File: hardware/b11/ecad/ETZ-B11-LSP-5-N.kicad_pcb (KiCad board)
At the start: 2 copper layers, 144.7 x 90.2 mm, 0 parts

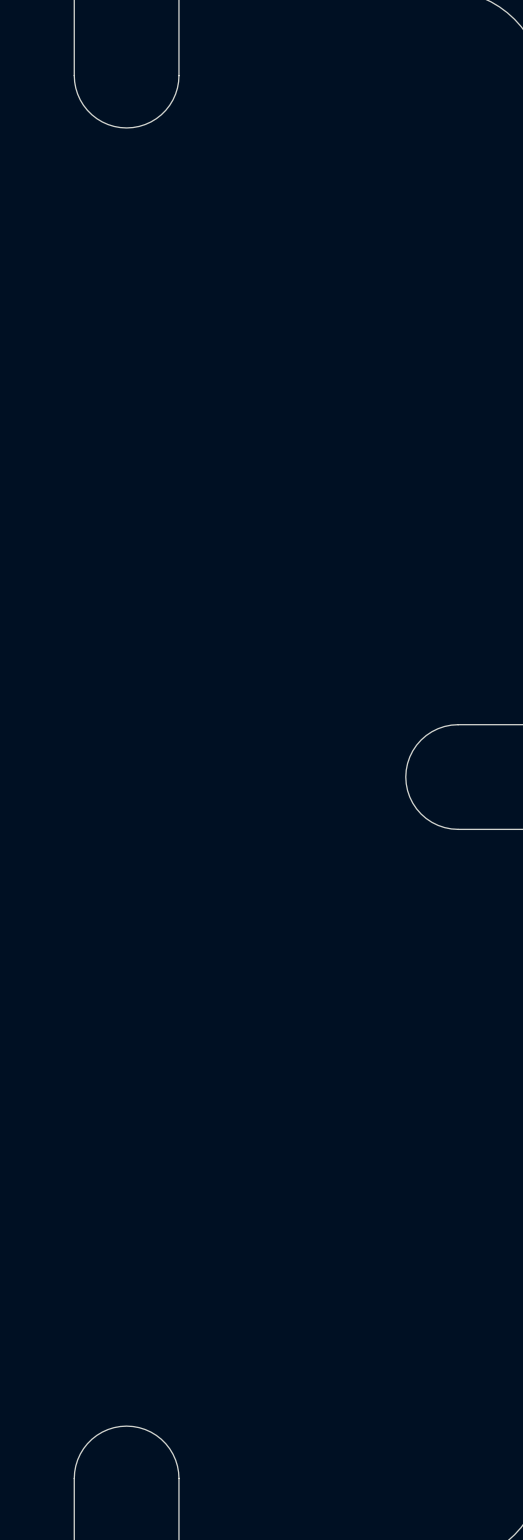
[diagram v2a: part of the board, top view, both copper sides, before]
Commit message: feat(hardware/b11): populate component placements across all carrier PCBs
KiCad serialized full footprint and component placement data for all
four carrier board variants after interactive editing session.

Co-Authored-By: Claude Sonnet 4.6 <noreply@anthropic.com>
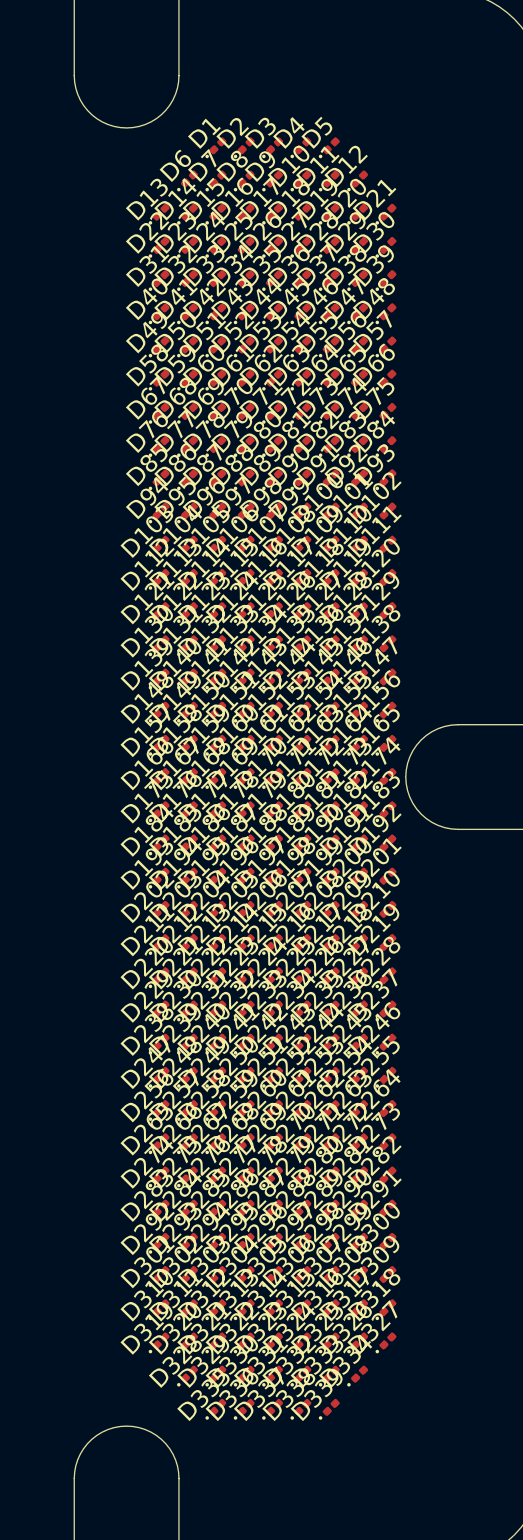
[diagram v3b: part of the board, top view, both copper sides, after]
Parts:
- added D1: LED_0201_0603Metric, LED_0201_0603Metric, F.Cu at (202.2, 68.1)
- added D10: LED_0201_0603Metric, LED_0201_0603Metric, F.Cu at (207.1, 70.0)
- added D100: LED_0201_0603Metric, LED_0201_0603Metric, F.Cu at (208.7, 89.1)
- added D101: LED_0201_0603Metric, LED_0201_0603Metric, F.Cu at (210.3, 89.1)
- added D102: LED_0201_0603Metric, LED_0201_0603Metric, F.Cu at (211.9, 89.1)
- added D103: LED_0201_0603Metric, LED_0201_0603Metric, F.Cu at (198.9, 91.0)
- added D104: LED_0201_0603Metric, LED_0201_0603Metric, F.Cu at (200.6, 91.0)
- added D105: LED_0201_0603Metric, LED_0201_0603Metric, F.Cu at (202.2, 91.0)
- added D106: LED_0201_0603Metric, LED_0201_0603Metric, F.Cu at (203.8, 91.0)
- added D107: LED_0201_0603Metric, LED_0201_0603Metric, F.Cu at (205.4, 91.0)
- added D108: LED_0201_0603Metric, LED_0201_0603Metric, F.Cu at (207.1, 91.0)
- added D109: LED_0201_0603Metric, LED_0201_0603Metric, F.Cu at (208.7, 91.0)
- added D11: LED_0201_0603Metric, LED_0201_0603Metric, F.Cu at (208.7, 70.0)
- added D110: LED_0201_0603Metric, LED_0201_0603Metric, F.Cu at (210.3, 91.0)
- added D111: LED_0201_0603Metric, LED_0201_0603Metric, F.Cu at (211.9, 91.0)
- added D112: LED_0201_0603Metric, LED_0201_0603Metric, F.Cu at (198.9, 92.9)
- added D113: LED_0201_0603Metric, LED_0201_0603Metric, F.Cu at (200.6, 92.9)
- added D114: LED_0201_0603Metric, LED_0201_0603Metric, F.Cu at (202.2, 92.9)
- added D115: LED_0201_0603Metric, LED_0201_0603Metric, F.Cu at (203.8, 92.9)
- added D116: LED_0201_0603Metric, LED_0201_0603Metric, F.Cu at (205.4, 92.9)
- added D117: LED_0201_0603Metric, LED_0201_0603Metric, F.Cu at (207.1, 92.9)
- added D118: LED_0201_0603Metric, LED_0201_0603Metric, F.Cu at (208.7, 92.9)
- added D119: LED_0201_0603Metric, LED_0201_0603Metric, F.Cu at (210.3, 92.9)
- added D12: LED_0201_0603Metric, LED_0201_0603Metric, F.Cu at (210.3, 70.0)
- added D120: LED_0201_0603Metric, LED_0201_0603Metric, F.Cu at (211.9, 92.9)
- added D121: LED_0201_0603Metric, LED_0201_0603Metric, F.Cu at (198.9, 94.8)
- added D122: LED_0201_0603Metric, LED_0201_0603Metric, F.Cu at (200.6, 94.8)
- added D123: LED_0201_0603Metric, LED_0201_0603Metric, F.Cu at (202.2, 94.8)
- added D124: LED_0201_0603Metric, LED_0201_0603Metric, F.Cu at (203.8, 94.8)
- added D125: LED_0201_0603Metric, LED_0201_0603Metric, F.Cu at (205.4, 94.8)
- added D126: LED_0201_0603Metric, LED_0201_0603Metric, F.Cu at (207.1, 94.8)
- added D127: LED_0201_0603Metric, LED_0201_0603Metric, F.Cu at (208.7, 94.8)
- added D128: LED_0201_0603Metric, LED_0201_0603Metric, F.Cu at (210.3, 94.8)
- added D129: LED_0201_0603Metric, LED_0201_0603Metric, F.Cu at (211.9, 94.8)
- added D13: LED_0201_0603Metric, LED_0201_0603Metric, F.Cu at (198.9, 71.9)
- added D130: LED_0201_0603Metric, LED_0201_0603Metric, F.Cu at (198.9, 96.7)
- added D131: LED_0201_0603Metric, LED_0201_0603Metric, F.Cu at (200.6, 96.7)
- added D132: LED_0201_0603Metric, LED_0201_0603Metric, F.Cu at (202.2, 96.7)
- added D133: LED_0201_0603Metric, LED_0201_0603Metric, F.Cu at (203.8, 96.7)
- added D134: LED_0201_0603Metric, LED_0201_0603Metric, F.Cu at (205.4, 96.7)
- added D135: LED_0201_0603Metric, LED_0201_0603Metric, F.Cu at (207.1, 96.7)
- added D136: LED_0201_0603Metric, LED_0201_0603Metric, F.Cu at (208.7, 96.7)
- added D137: LED_0201_0603Metric, LED_0201_0603Metric, F.Cu at (210.3, 96.7)
- added D138: LED_0201_0603Metric, LED_0201_0603Metric, F.Cu at (211.9, 96.7)
- added D139: LED_0201_0603Metric, LED_0201_0603Metric, F.Cu at (198.9, 98.6)
- added D14: LED_0201_0603Metric, LED_0201_0603Metric, F.Cu at (200.6, 71.9)
- added D140: LED_0201_0603Metric, LED_0201_0603Metric, F.Cu at (200.6, 98.6)
- added D141: LED_0201_0603Metric, LED_0201_0603Metric, F.Cu at (202.2, 98.6)
- added D142: LED_0201_0603Metric, LED_0201_0603Metric, F.Cu at (203.8, 98.6)
- added D143: LED_0201_0603Metric, LED_0201_0603Metric, F.Cu at (205.4, 98.6)
- added D144: LED_0201_0603Metric, LED_0201_0603Metric, F.Cu at (207.1, 98.6)
- added D145: LED_0201_0603Metric, LED_0201_0603Metric, F.Cu at (208.7, 98.6)
- added D146: LED_0201_0603Metric, LED_0201_0603Metric, F.Cu at (210.3, 98.6)
- added D147: LED_0201_0603Metric, LED_0201_0603Metric, F.Cu at (211.9, 98.6)
- added D148: LED_0201_0603Metric, LED_0201_0603Metric, F.Cu at (198.9, 100.5)
- added D149: LED_0201_0603Metric, LED_0201_0603Metric, F.Cu at (200.6, 100.5)
- added D15: LED_0201_0603Metric, LED_0201_0603Metric, F.Cu at (202.2, 71.9)
- added D150: LED_0201_0603Metric, LED_0201_0603Metric, F.Cu at (202.2, 100.5)
- added D151: LED_0201_0603Metric, LED_0201_0603Metric, F.Cu at (203.8, 100.5)
- added D152: LED_0201_0603Metric, LED_0201_0603Metric, F.Cu at (205.4, 100.5)
- added D153: LED_0201_0603Metric, LED_0201_0603Metric, F.Cu at (207.1, 100.5)
- added D154: LED_0201_0603Metric, LED_0201_0603Metric, F.Cu at (208.7, 100.5)
- added D155: LED_0201_0603Metric, LED_0201_0603Metric, F.Cu at (210.3, 100.5)
- added D156: LED_0201_0603Metric, LED_0201_0603Metric, F.Cu at (211.9, 100.5)
- added D157: LED_0201_0603Metric, LED_0201_0603Metric, F.Cu at (198.9, 102.4)
- added D158: LED_0201_0603Metric, LED_0201_0603Metric, F.Cu at (200.6, 102.4)
- added D159: LED_0201_0603Metric, LED_0201_0603Metric, F.Cu at (202.2, 102.4)
- added D16: LED_0201_0603Metric, LED_0201_0603Metric, F.Cu at (203.8, 71.9)
- added D160: LED_0201_0603Metric, LED_0201_0603Metric, F.Cu at (203.8, 102.4)
- added D161: LED_0201_0603Metric, LED_0201_0603Metric, F.Cu at (205.4, 102.4)
- added D162: LED_0201_0603Metric, LED_0201_0603Metric, F.Cu at (207.1, 102.4)
- added D163: LED_0201_0603Metric, LED_0201_0603Metric, F.Cu at (208.7, 102.4)
- added D164: LED_0201_0603Metric, LED_0201_0603Metric, F.Cu at (210.3, 102.4)
- added D165: LED_0201_0603Metric, LED_0201_0603Metric, F.Cu at (211.9, 102.4)
- added D166: LED_0201_0603Metric, LED_0201_0603Metric, F.Cu at (198.9, 104.3)
- added D167: LED_0201_0603Metric, LED_0201_0603Metric, F.Cu at (200.6, 104.3)
- added D168: LED_0201_0603Metric, LED_0201_0603Metric, F.Cu at (202.2, 104.3)
- added D169: LED_0201_0603Metric, LED_0201_0603Metric, F.Cu at (203.8, 104.3)
- added D17: LED_0201_0603Metric, LED_0201_0603Metric, F.Cu at (205.4, 71.9)
- added D170: LED_0201_0603Metric, LED_0201_0603Metric, F.Cu at (205.4, 104.3)
- added D171: LED_0201_0603Metric, LED_0201_0603Metric, F.Cu at (207.1, 104.3)
- added D172: LED_0201_0603Metric, LED_0201_0603Metric, F.Cu at (208.7, 104.3)
- added D173: LED_0201_0603Metric, LED_0201_0603Metric, F.Cu at (210.3, 104.3)
- added D174: LED_0201_0603Metric, LED_0201_0603Metric, F.Cu at (211.9, 104.3)
- added D175: LED_0201_0603Metric, LED_0201_0603Metric, F.Cu at (198.9, 106.2)
- added D176: LED_0201_0603Metric, LED_0201_0603Metric, F.Cu at (200.6, 106.2)
- added D177: LED_0201_0603Metric, LED_0201_0603Metric, F.Cu at (202.2, 106.2)
- added D178: LED_0201_0603Metric, LED_0201_0603Metric, F.Cu at (203.8, 106.2)
- added D179: LED_0201_0603Metric, LED_0201_0603Metric, F.Cu at (205.4, 106.2)
- added D18: LED_0201_0603Metric, LED_0201_0603Metric, F.Cu at (207.1, 71.9)
- added D180: LED_0201_0603Metric, LED_0201_0603Metric, F.Cu at (207.1, 106.2)
- added D181: LED_0201_0603Metric, LED_0201_0603Metric, F.Cu at (208.7, 106.2)
- added D182: LED_0201_0603Metric, LED_0201_0603Metric, F.Cu at (210.3, 106.2)
- added D183: LED_0201_0603Metric, LED_0201_0603Metric, F.Cu at (211.9, 106.2)
- added D184: LED_0201_0603Metric, LED_0201_0603Metric, F.Cu at (198.9, 108.1)
- added D185: LED_0201_0603Metric, LED_0201_0603Metric, F.Cu at (200.6, 108.1)
- added D186: LED_0201_0603Metric, LED_0201_0603Metric, F.Cu at (202.2, 108.1)
- added D187: LED_0201_0603Metric, LED_0201_0603Metric, F.Cu at (203.8, 108.1)
- added D188: LED_0201_0603Metric, LED_0201_0603Metric, F.Cu at (205.4, 108.1)
- added D189: LED_0201_0603Metric, LED_0201_0603Metric, F.Cu at (207.1, 108.1)
- added D19: LED_0201_0603Metric, LED_0201_0603Metric, F.Cu at (208.7, 71.9)
- added D190: LED_0201_0603Metric, LED_0201_0603Metric, F.Cu at (208.7, 108.1)
- added D191: LED_0201_0603Metric, LED_0201_0603Metric, F.Cu at (210.3, 108.1)
- added D192: LED_0201_0603Metric, LED_0201_0603Metric, F.Cu at (211.9, 108.1)
- added D193: LED_0201_0603Metric, LED_0201_0603Metric, F.Cu at (198.9, 110.0)
- added D194: LED_0201_0603Metric, LED_0201_0603Metric, F.Cu at (200.6, 110.0)
- added D195: LED_0201_0603Metric, LED_0201_0603Metric, F.Cu at (202.2, 110.0)
- added D196: LED_0201_0603Metric, LED_0201_0603Metric, F.Cu at (203.8, 110.0)
- added D197: LED_0201_0603Metric, LED_0201_0603Metric, F.Cu at (205.4, 110.0)
- added D198: LED_0201_0603Metric, LED_0201_0603Metric, F.Cu at (207.1, 110.0)
- added D199: LED_0201_0603Metric, LED_0201_0603Metric, F.Cu at (208.7, 110.0)
- added D2: LED_0201_0603Metric, LED_0201_0603Metric, F.Cu at (203.8, 68.1)
- added D20: LED_0201_0603Metric, LED_0201_0603Metric, F.Cu at (210.3, 71.9)
- added D200: LED_0201_0603Metric, LED_0201_0603Metric, F.Cu at (210.3, 110.0)
- added D201: LED_0201_0603Metric, LED_0201_0603Metric, F.Cu at (211.9, 110.0)
- added D202: LED_0201_0603Metric, LED_0201_0603Metric, F.Cu at (198.9, 111.9)
- added D203: LED_0201_0603Metric, LED_0201_0603Metric, F.Cu at (200.6, 111.9)
- added D204: LED_0201_0603Metric, LED_0201_0603Metric, F.Cu at (202.2, 111.9)
- added D205: LED_0201_0603Metric, LED_0201_0603Metric, F.Cu at (203.8, 111.9)
- added D206: LED_0201_0603Metric, LED_0201_0603Metric, F.Cu at (205.4, 111.9)
- added D207: LED_0201_0603Metric, LED_0201_0603Metric, F.Cu at (207.1, 111.9)
- added D208: LED_0201_0603Metric, LED_0201_0603Metric, F.Cu at (208.7, 111.9)
- added D209: LED_0201_0603Metric, LED_0201_0603Metric, F.Cu at (210.3, 111.9)
- added D21: LED_0201_0603Metric, LED_0201_0603Metric, F.Cu at (211.9, 71.9)
- added D210: LED_0201_0603Metric, LED_0201_0603Metric, F.Cu at (211.9, 111.9)
- added D211: LED_0201_0603Metric, LED_0201_0603Metric, F.Cu at (198.9, 113.8)
- added D212: LED_0201_0603Metric, LED_0201_0603Metric, F.Cu at (200.6, 113.8)
- added D213: LED_0201_0603Metric, LED_0201_0603Metric, F.Cu at (202.2, 113.8)
- added D214: LED_0201_0603Metric, LED_0201_0603Metric, F.Cu at (203.8, 113.8)
- added D215: LED_0201_0603Metric, LED_0201_0603Metric, F.Cu at (205.4, 113.8)
- added D216: LED_0201_0603Metric, LED_0201_0603Metric, F.Cu at (207.1, 113.8)
- added D217: LED_0201_0603Metric, LED_0201_0603Metric, F.Cu at (208.7, 113.8)
- added D218: LED_0201_0603Metric, LED_0201_0603Metric, F.Cu at (210.3, 113.8)
- added D219: LED_0201_0603Metric, LED_0201_0603Metric, F.Cu at (211.9, 113.8)
- added D22: LED_0201_0603Metric, LED_0201_0603Metric, F.Cu at (198.9, 73.8)
- added D220: LED_0201_0603Metric, LED_0201_0603Metric, F.Cu at (198.9, 115.7)
- added D221: LED_0201_0603Metric, LED_0201_0603Metric, F.Cu at (200.6, 115.7)
- added D222: LED_0201_0603Metric, LED_0201_0603Metric, F.Cu at (202.2, 115.7)
- added D223: LED_0201_0603Metric, LED_0201_0603Metric, F.Cu at (203.8, 115.7)
- added D224: LED_0201_0603Metric, LED_0201_0603Metric, F.Cu at (205.4, 115.7)
- added D225: LED_0201_0603Metric, LED_0201_0603Metric, F.Cu at (207.1, 115.7)
- added D226: LED_0201_0603Metric, LED_0201_0603Metric, F.Cu at (208.7, 115.7)
- added D227: LED_0201_0603Metric, LED_0201_0603Metric, F.Cu at (210.3, 115.7)
- added D228: LED_0201_0603Metric, LED_0201_0603Metric, F.Cu at (211.9, 115.7)
- added D229: LED_0201_0603Metric, LED_0201_0603Metric, F.Cu at (198.9, 117.6)
- added D23: LED_0201_0603Metric, LED_0201_0603Metric, F.Cu at (200.6, 73.8)
- added D230: LED_0201_0603Metric, LED_0201_0603Metric, F.Cu at (200.6, 117.6)
- added D231: LED_0201_0603Metric, LED_0201_0603Metric, F.Cu at (202.2, 117.6)
- added D232: LED_0201_0603Metric, LED_0201_0603Metric, F.Cu at (203.8, 117.6)
- added D233: LED_0201_0603Metric, LED_0201_0603Metric, F.Cu at (205.4, 117.6)
- added D234: LED_0201_0603Metric, LED_0201_0603Metric, F.Cu at (207.1, 117.6)
- added D235: LED_0201_0603Metric, LED_0201_0603Metric, F.Cu at (208.7, 117.6)
- added D236: LED_0201_0603Metric, LED_0201_0603Metric, F.Cu at (210.3, 117.6)
- added D237: LED_0201_0603Metric, LED_0201_0603Metric, F.Cu at (211.9, 117.6)
- added D238: LED_0201_0603Metric, LED_0201_0603Metric, F.Cu at (198.9, 119.5)
- added D239: LED_0201_0603Metric, LED_0201_0603Metric, F.Cu at (200.6, 119.5)
- added D24: LED_0201_0603Metric, LED_0201_0603Metric, F.Cu at (202.2, 73.8)
- added D240: LED_0201_0603Metric, LED_0201_0603Metric, F.Cu at (202.2, 119.5)
- added D241: LED_0201_0603Metric, LED_0201_0603Metric, F.Cu at (203.8, 119.5)
- added D242: LED_0201_0603Metric, LED_0201_0603Metric, F.Cu at (205.4, 119.5)
- added D243: LED_0201_0603Metric, LED_0201_0603Metric, F.Cu at (207.1, 119.5)
- added D244: LED_0201_0603Metric, LED_0201_0603Metric, F.Cu at (208.7, 119.5)
- added D245: LED_0201_0603Metric, LED_0201_0603Metric, F.Cu at (210.3, 119.5)
- added D246: LED_0201_0603Metric, LED_0201_0603Metric, F.Cu at (211.9, 119.5)
- added D247: LED_0201_0603Metric, LED_0201_0603Metric, F.Cu at (198.9, 121.4)
- added D248: LED_0201_0603Metric, LED_0201_0603Metric, F.Cu at (200.6, 121.4)
- added D249: LED_0201_0603Metric, LED_0201_0603Metric, F.Cu at (202.2, 121.4)
- added D25: LED_0201_0603Metric, LED_0201_0603Metric, F.Cu at (203.8, 73.8)
- added D250: LED_0201_0603Metric, LED_0201_0603Metric, F.Cu at (203.8, 121.4)
- added D251: LED_0201_0603Metric, LED_0201_0603Metric, F.Cu at (205.4, 121.4)
- added D252: LED_0201_0603Metric, LED_0201_0603Metric, F.Cu at (207.1, 121.4)
- added D253: LED_0201_0603Metric, LED_0201_0603Metric, F.Cu at (208.7, 121.4)
- added D254: LED_0201_0603Metric, LED_0201_0603Metric, F.Cu at (210.3, 121.4)
- added D255: LED_0201_0603Metric, LED_0201_0603Metric, F.Cu at (211.9, 121.4)
- added D256: LED_0201_0603Metric, LED_0201_0603Metric, F.Cu at (198.9, 123.3)
- added D257: LED_0201_0603Metric, LED_0201_0603Metric, F.Cu at (200.6, 123.3)
- added D258: LED_0201_0603Metric, LED_0201_0603Metric, F.Cu at (202.2, 123.3)
- added D259: LED_0201_0603Metric, LED_0201_0603Metric, F.Cu at (203.8, 123.3)
- added D26: LED_0201_0603Metric, LED_0201_0603Metric, F.Cu at (205.4, 73.8)
- added D260: LED_0201_0603Metric, LED_0201_0603Metric, F.Cu at (205.4, 123.3)
- added D261: LED_0201_0603Metric, LED_0201_0603Metric, F.Cu at (207.1, 123.3)
- added D262: LED_0201_0603Metric, LED_0201_0603Metric, F.Cu at (208.7, 123.3)
- added D263: LED_0201_0603Metric, LED_0201_0603Metric, F.Cu at (210.3, 123.3)
- added D264: LED_0201_0603Metric, LED_0201_0603Metric, F.Cu at (211.9, 123.3)
- added D265: LED_0201_0603Metric, LED_0201_0603Metric, F.Cu at (198.9, 125.2)
- added D266: LED_0201_0603Metric, LED_0201_0603Metric, F.Cu at (200.6, 125.2)
- added D267: LED_0201_0603Metric, LED_0201_0603Metric, F.Cu at (202.2, 125.2)
- added D268: LED_0201_0603Metric, LED_0201_0603Metric, F.Cu at (203.8, 125.2)
- added D269: LED_0201_0603Metric, LED_0201_0603Metric, F.Cu at (205.4, 125.2)
- added D27: LED_0201_0603Metric, LED_0201_0603Metric, F.Cu at (207.1, 73.8)
- added D270: LED_0201_0603Metric, LED_0201_0603Metric, F.Cu at (207.1, 125.2)
- added D271: LED_0201_0603Metric, LED_0201_0603Metric, F.Cu at (208.7, 125.2)
- added D272: LED_0201_0603Metric, LED_0201_0603Metric, F.Cu at (210.3, 125.2)
- added D273: LED_0201_0603Metric, LED_0201_0603Metric, F.Cu at (211.9, 125.2)
- added D274: LED_0201_0603Metric, LED_0201_0603Metric, F.Cu at (198.9, 127.1)
- added D275: LED_0201_0603Metric, LED_0201_0603Metric, F.Cu at (200.6, 127.1)
- added D276: LED_0201_0603Metric, LED_0201_0603Metric, F.Cu at (202.2, 127.1)
- added D277: LED_0201_0603Metric, LED_0201_0603Metric, F.Cu at (203.8, 127.1)
- added D278: LED_0201_0603Metric, LED_0201_0603Metric, F.Cu at (205.4, 127.1)
- added D279: LED_0201_0603Metric, LED_0201_0603Metric, F.Cu at (207.1, 127.1)
- added D28: LED_0201_0603Metric, LED_0201_0603Metric, F.Cu at (208.7, 73.8)
- added D280: LED_0201_0603Metric, LED_0201_0603Metric, F.Cu at (208.7, 127.1)
- added D281: LED_0201_0603Metric, LED_0201_0603Metric, F.Cu at (210.3, 127.1)
- added D282: LED_0201_0603Metric, LED_0201_0603Metric, F.Cu at (211.9, 127.1)
- added D283: LED_0201_0603Metric, LED_0201_0603Metric, F.Cu at (198.9, 129.0)
- added D284: LED_0201_0603Metric, LED_0201_0603Metric, F.Cu at (200.6, 129.0)
- added D285: LED_0201_0603Metric, LED_0201_0603Metric, F.Cu at (202.2, 129.0)
- added D286: LED_0201_0603Metric, LED_0201_0603Metric, F.Cu at (203.8, 129.0)
- added D287: LED_0201_0603Metric, LED_0201_0603Metric, F.Cu at (205.4, 129.0)
- added D288: LED_0201_0603Metric, LED_0201_0603Metric, F.Cu at (207.1, 129.0)
- added D289: LED_0201_0603Metric, LED_0201_0603Metric, F.Cu at (208.7, 129.0)
- added D29: LED_0201_0603Metric, LED_0201_0603Metric, F.Cu at (210.3, 73.8)
- added D290: LED_0201_0603Metric, LED_0201_0603Metric, F.Cu at (210.3, 129.0)
- added D291: LED_0201_0603Metric, LED_0201_0603Metric, F.Cu at (211.9, 129.0)
- added D292: LED_0201_0603Metric, LED_0201_0603Metric, F.Cu at (198.9, 130.9)
- added D293: LED_0201_0603Metric, LED_0201_0603Metric, F.Cu at (200.6, 130.9)
- added D294: LED_0201_0603Metric, LED_0201_0603Metric, F.Cu at (202.2, 130.9)
- added D295: LED_0201_0603Metric, LED_0201_0603Metric, F.Cu at (203.8, 130.9)
- added D296: LED_0201_0603Metric, LED_0201_0603Metric, F.Cu at (205.4, 130.9)
- added D297: LED_0201_0603Metric, LED_0201_0603Metric, F.Cu at (207.1, 130.9)
- added D298: LED_0201_0603Metric, LED_0201_0603Metric, F.Cu at (208.7, 130.9)
- added D299: LED_0201_0603Metric, LED_0201_0603Metric, F.Cu at (210.3, 130.9)
- added D3: LED_0201_0603Metric, LED_0201_0603Metric, F.Cu at (205.4, 68.1)
- added D30: LED_0201_0603Metric, LED_0201_0603Metric, F.Cu at (211.9, 73.8)
- added D300: LED_0201_0603Metric, LED_0201_0603Metric, F.Cu at (211.9, 130.9)
- added D301: LED_0201_0603Metric, LED_0201_0603Metric, F.Cu at (198.9, 132.8)
- added D302: LED_0201_0603Metric, LED_0201_0603Metric, F.Cu at (200.6, 132.8)
- added D303: LED_0201_0603Metric, LED_0201_0603Metric, F.Cu at (202.2, 132.8)
- added D304: LED_0201_0603Metric, LED_0201_0603Metric, F.Cu at (203.8, 132.8)
- added D305: LED_0201_0603Metric, LED_0201_0603Metric, F.Cu at (205.4, 132.8)
- added D306: LED_0201_0603Metric, LED_0201_0603Metric, F.Cu at (207.1, 132.8)
- added D307: LED_0201_0603Metric, LED_0201_0603Metric, F.Cu at (208.7, 132.8)
- added D308: LED_0201_0603Metric, LED_0201_0603Metric, F.Cu at (210.3, 132.8)
- added D309: LED_0201_0603Metric, LED_0201_0603Metric, F.Cu at (211.9, 132.8)
- added D31: LED_0201_0603Metric, LED_0201_0603Metric, F.Cu at (198.9, 75.7)
- added D310: LED_0201_0603Metric, LED_0201_0603Metric, F.Cu at (198.9, 134.7)
- added D311: LED_0201_0603Metric, LED_0201_0603Metric, F.Cu at (200.6, 134.7)
- added D312: LED_0201_0603Metric, LED_0201_0603Metric, F.Cu at (202.2, 134.7)
- added D313: LED_0201_0603Metric, LED_0201_0603Metric, F.Cu at (203.8, 134.7)
- added D314: LED_0201_0603Metric, LED_0201_0603Metric, F.Cu at (205.4, 134.7)
- added D315: LED_0201_0603Metric, LED_0201_0603Metric, F.Cu at (207.1, 134.7)
- added D316: LED_0201_0603Metric, LED_0201_0603Metric, F.Cu at (208.7, 134.7)
- added D317: LED_0201_0603Metric, LED_0201_0603Metric, F.Cu at (210.3, 134.7)
- added D318: LED_0201_0603Metric, LED_0201_0603Metric, F.Cu at (211.9, 134.7)
- added D319: LED_0201_0603Metric, LED_0201_0603Metric, F.Cu at (198.9, 136.6)
- added D32: LED_0201_0603Metric, LED_0201_0603Metric, F.Cu at (200.6, 75.7)
- added D320: LED_0201_0603Metric, LED_0201_0603Metric, F.Cu at (200.6, 136.6)
- added D321: LED_0201_0603Metric, LED_0201_0603Metric, F.Cu at (202.2, 136.6)
- added D322: LED_0201_0603Metric, LED_0201_0603Metric, F.Cu at (203.8, 136.6)
- added D323: LED_0201_0603Metric, LED_0201_0603Metric, F.Cu at (205.4, 136.6)
- added D324: LED_0201_0603Metric, LED_0201_0603Metric, F.Cu at (207.1, 136.6)
- added D325: LED_0201_0603Metric, LED_0201_0603Metric, F.Cu at (208.7, 136.6)
- added D326: LED_0201_0603Metric, LED_0201_0603Metric, F.Cu at (210.3, 136.6)
- added D327: LED_0201_0603Metric, LED_0201_0603Metric, F.Cu at (211.9, 136.6)
- added D328: LED_0201_0603Metric, LED_0201_0603Metric, F.Cu at (200.6, 138.5)
- added D329: LED_0201_0603Metric, LED_0201_0603Metric, F.Cu at (202.2, 138.5)
- added D33: LED_0201_0603Metric, LED_0201_0603Metric, F.Cu at (202.2, 75.7)
- added D330: LED_0201_0603Metric, LED_0201_0603Metric, F.Cu at (203.8, 138.5)
- added D331: LED_0201_0603Metric, LED_0201_0603Metric, F.Cu at (205.4, 138.5)
- added D332: LED_0201_0603Metric, LED_0201_0603Metric, F.Cu at (207.1, 138.5)
- added D333: LED_0201_0603Metric, LED_0201_0603Metric, F.Cu at (208.7, 138.5)
- added D334: LED_0201_0603Metric, LED_0201_0603Metric, F.Cu at (210.3, 138.5)
- added D335: LED_0201_0603Metric, LED_0201_0603Metric, F.Cu at (202.2, 140.4)
- added D336: LED_0201_0603Metric, LED_0201_0603Metric, F.Cu at (203.8, 140.4)
- added D337: LED_0201_0603Metric, LED_0201_0603Metric, F.Cu at (205.4, 140.4)
- added D338: LED_0201_0603Metric, LED_0201_0603Metric, F.Cu at (207.1, 140.4)
- added D339: LED_0201_0603Metric, LED_0201_0603Metric, F.Cu at (208.7, 140.4)
- added D34: LED_0201_0603Metric, LED_0201_0603Metric, F.Cu at (203.8, 75.7)
- added D35: LED_0201_0603Metric, LED_0201_0603Metric, F.Cu at (205.4, 75.7)
- added D36: LED_0201_0603Metric, LED_0201_0603Metric, F.Cu at (207.1, 75.7)
- added D37: LED_0201_0603Metric, LED_0201_0603Metric, F.Cu at (208.7, 75.7)
- added D38: LED_0201_0603Metric, LED_0201_0603Metric, F.Cu at (210.3, 75.7)
- added D39: LED_0201_0603Metric, LED_0201_0603Metric, F.Cu at (211.9, 75.7)
- added D4: LED_0201_0603Metric, LED_0201_0603Metric, F.Cu at (207.1, 68.1)
- added D40: LED_0201_0603Metric, LED_0201_0603Metric, F.Cu at (198.9, 77.6)
- added D41: LED_0201_0603Metric, LED_0201_0603Metric, F.Cu at (200.6, 77.6)
- added D42: LED_0201_0603Metric, LED_0201_0603Metric, F.Cu at (202.2, 77.6)
- added D43: LED_0201_0603Metric, LED_0201_0603Metric, F.Cu at (203.8, 77.6)
- added D44: LED_0201_0603Metric, LED_0201_0603Metric, F.Cu at (205.4, 77.6)
- added D45: LED_0201_0603Metric, LED_0201_0603Metric, F.Cu at (207.1, 77.6)
- added D46: LED_0201_0603Metric, LED_0201_0603Metric, F.Cu at (208.7, 77.6)
- added D47: LED_0201_0603Metric, LED_0201_0603Metric, F.Cu at (210.3, 77.6)
- added D48: LED_0201_0603Metric, LED_0201_0603Metric, F.Cu at (211.9, 77.6)
- added D49: LED_0201_0603Metric, LED_0201_0603Metric, F.Cu at (198.9, 79.5)
- added D5: LED_0201_0603Metric, LED_0201_0603Metric, F.Cu at (208.7, 68.1)
- added D50: LED_0201_0603Metric, LED_0201_0603Metric, F.Cu at (200.6, 79.5)
- added D51: LED_0201_0603Metric, LED_0201_0603Metric, F.Cu at (202.2, 79.5)
- added D52: LED_0201_0603Metric, LED_0201_0603Metric, F.Cu at (203.8, 79.5)
- added D53: LED_0201_0603Metric, LED_0201_0603Metric, F.Cu at (205.4, 79.5)
- added D54: LED_0201_0603Metric, LED_0201_0603Metric, F.Cu at (207.1, 79.5)
- added D55: LED_0201_0603Metric, LED_0201_0603Metric, F.Cu at (208.7, 79.5)
- added D56: LED_0201_0603Metric, LED_0201_0603Metric, F.Cu at (210.3, 79.5)
- added D57: LED_0201_0603Metric, LED_0201_0603Metric, F.Cu at (211.9, 79.5)
- added D58: LED_0201_0603Metric, LED_0201_0603Metric, F.Cu at (198.9, 81.4)
- added D59: LED_0201_0603Metric, LED_0201_0603Metric, F.Cu at (200.6, 81.4)
- added D6: LED_0201_0603Metric, LED_0201_0603Metric, F.Cu at (200.6, 70.0)
- added D60: LED_0201_0603Metric, LED_0201_0603Metric, F.Cu at (202.2, 81.4)
- added D61: LED_0201_0603Metric, LED_0201_0603Metric, F.Cu at (203.8, 81.4)
- added D62: LED_0201_0603Metric, LED_0201_0603Metric, F.Cu at (205.4, 81.4)
- added D63: LED_0201_0603Metric, LED_0201_0603Metric, F.Cu at (207.1, 81.4)
- added D64: LED_0201_0603Metric, LED_0201_0603Metric, F.Cu at (208.7, 81.4)
- added D65: LED_0201_0603Metric, LED_0201_0603Metric, F.Cu at (210.3, 81.4)
- added D66: LED_0201_0603Metric, LED_0201_0603Metric, F.Cu at (211.9, 81.4)
- added D67: LED_0201_0603Metric, LED_0201_0603Metric, F.Cu at (198.9, 83.3)
- added D68: LED_0201_0603Metric, LED_0201_0603Metric, F.Cu at (200.6, 83.3)
- added D69: LED_0201_0603Metric, LED_0201_0603Metric, F.Cu at (202.2, 83.3)
- added D7: LED_0201_0603Metric, LED_0201_0603Metric, F.Cu at (202.2, 70.0)
- added D70: LED_0201_0603Metric, LED_0201_0603Metric, F.Cu at (203.8, 83.3)
- added D71: LED_0201_0603Metric, LED_0201_0603Metric, F.Cu at (205.4, 83.3)
- added D72: LED_0201_0603Metric, LED_0201_0603Metric, F.Cu at (207.1, 83.3)
- added D73: LED_0201_0603Metric, LED_0201_0603Metric, F.Cu at (208.7, 83.3)
- added D74: LED_0201_0603Metric, LED_0201_0603Metric, F.Cu at (210.3, 83.3)
- added D75: LED_0201_0603Metric, LED_0201_0603Metric, F.Cu at (211.9, 83.3)
- added D76: LED_0201_0603Metric, LED_0201_0603Metric, F.Cu at (198.9, 85.2)
- added D77: LED_0201_0603Metric, LED_0201_0603Metric, F.Cu at (200.6, 85.2)
- added D78: LED_0201_0603Metric, LED_0201_0603Metric, F.Cu at (202.2, 85.2)
- added D79: LED_0201_0603Metric, LED_0201_0603Metric, F.Cu at (203.8, 85.2)
- added D8: LED_0201_0603Metric, LED_0201_0603Metric, F.Cu at (203.8, 70.0)
- added D80: LED_0201_0603Metric, LED_0201_0603Metric, F.Cu at (205.4, 85.2)
- added D81: LED_0201_0603Metric, LED_0201_0603Metric, F.Cu at (207.1, 85.2)
- added D82: LED_0201_0603Metric, LED_0201_0603Metric, F.Cu at (208.7, 85.2)
- added D83: LED_0201_0603Metric, LED_0201_0603Metric, F.Cu at (210.3, 85.2)
- added D84: LED_0201_0603Metric, LED_0201_0603Metric, F.Cu at (211.9, 85.2)
- added D85: LED_0201_0603Metric, LED_0201_0603Metric, F.Cu at (198.9, 87.2)
- added D86: LED_0201_0603Metric, LED_0201_0603Metric, F.Cu at (200.6, 87.2)
- added D87: LED_0201_0603Metric, LED_0201_0603Metric, F.Cu at (202.2, 87.2)
- added D88: LED_0201_0603Metric, LED_0201_0603Metric, F.Cu at (203.8, 87.2)
- added D89: LED_0201_0603Metric, LED_0201_0603Metric, F.Cu at (205.4, 87.2)
- added D9: LED_0201_0603Metric, LED_0201_0603Metric, F.Cu at (205.4, 70.0)
- added D90: LED_0201_0603Metric, LED_0201_0603Metric, F.Cu at (207.1, 87.2)
- added D91: LED_0201_0603Metric, LED_0201_0603Metric, F.Cu at (208.7, 87.2)
- added D92: LED_0201_0603Metric, LED_0201_0603Metric, F.Cu at (210.3, 87.2)
- added D93: LED_0201_0603Metric, LED_0201_0603Metric, F.Cu at (211.9, 87.2)
- added D94: LED_0201_0603Metric, LED_0201_0603Metric, F.Cu at (198.9, 89.1)
- added D95: LED_0201_0603Metric, LED_0201_0603Metric, F.Cu at (200.6, 89.1)
- added D96: LED_0201_0603Metric, LED_0201_0603Metric, F.Cu at (202.2, 89.1)
- added D97: LED_0201_0603Metric, LED_0201_0603Metric, F.Cu at (203.8, 89.1)
- added D98: LED_0201_0603Metric, LED_0201_0603Metric, F.Cu at (205.4, 89.1)
- added D99: LED_0201_0603Metric, LED_0201_0603Metric, F.Cu at (207.1, 89.1)
